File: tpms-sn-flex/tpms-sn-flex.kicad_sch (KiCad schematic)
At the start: 59 parts, among them J1 NRF_CONN, J2 DEBUG_CONN, J3 SMA EDGE CONN, J4 UART_CONN, J5 USER_CAP, J6 PRESSURE_SENSOR_CONN, SW1 SW_Push, U1 STM32U031R8T6

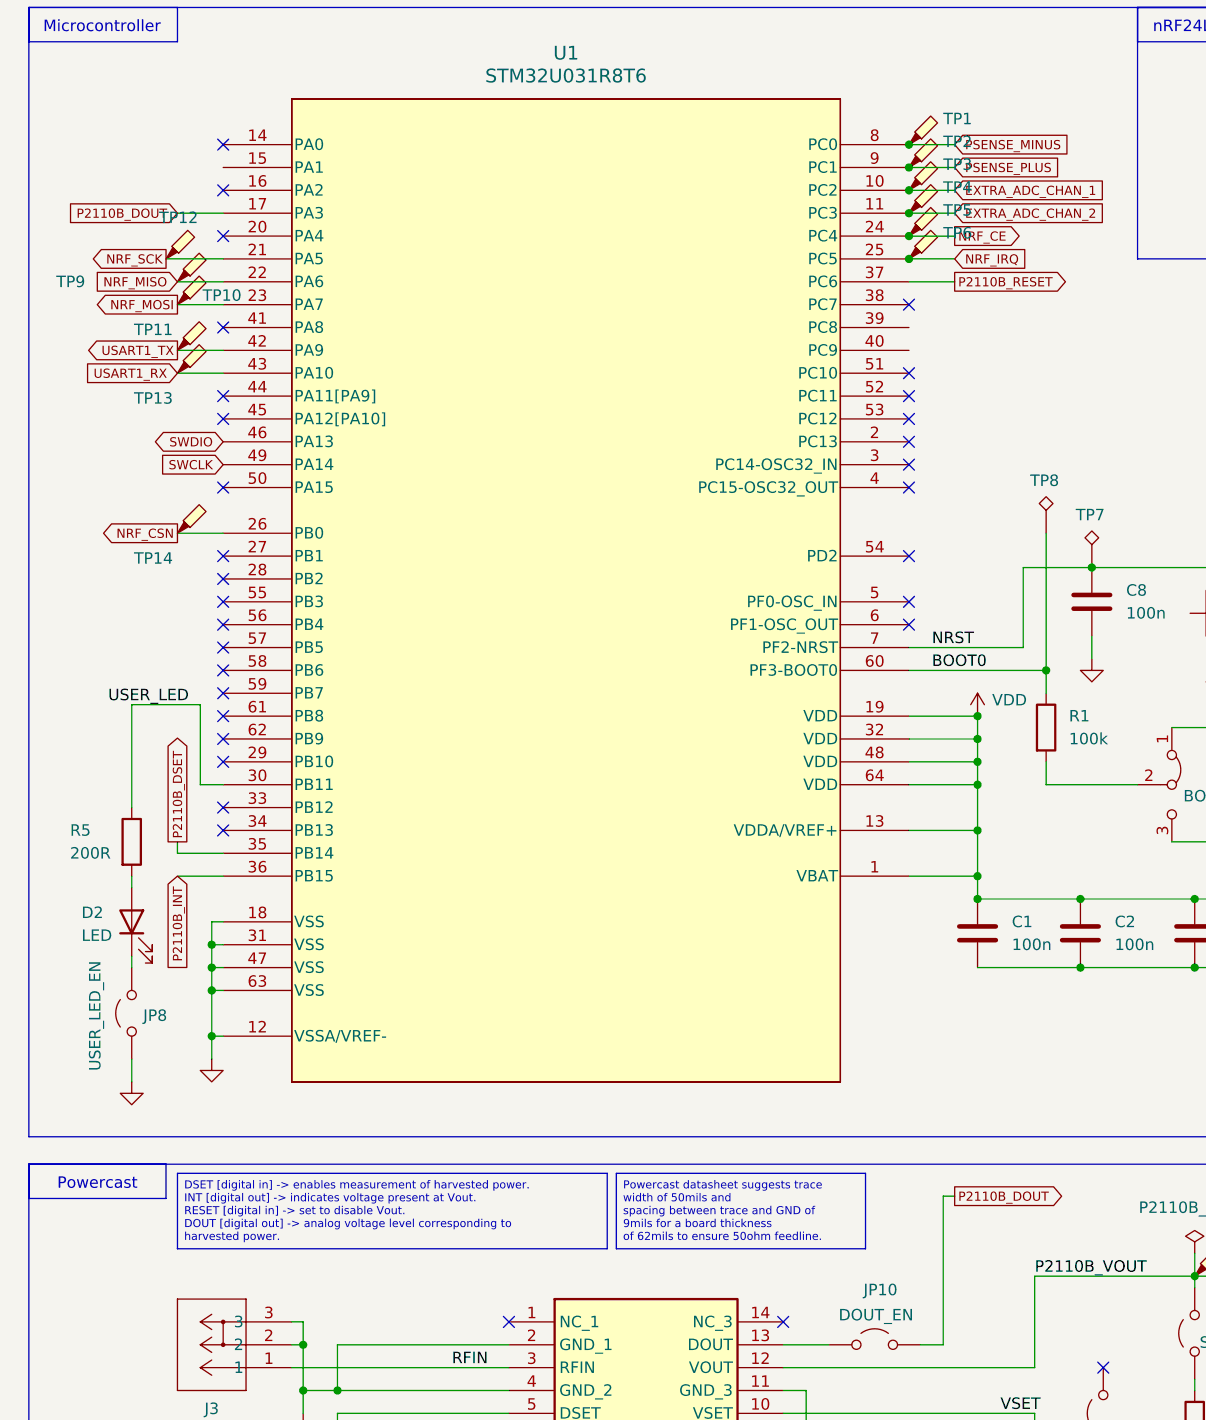
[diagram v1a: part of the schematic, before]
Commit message: Update PCB with silkscreen and fix DRC violations
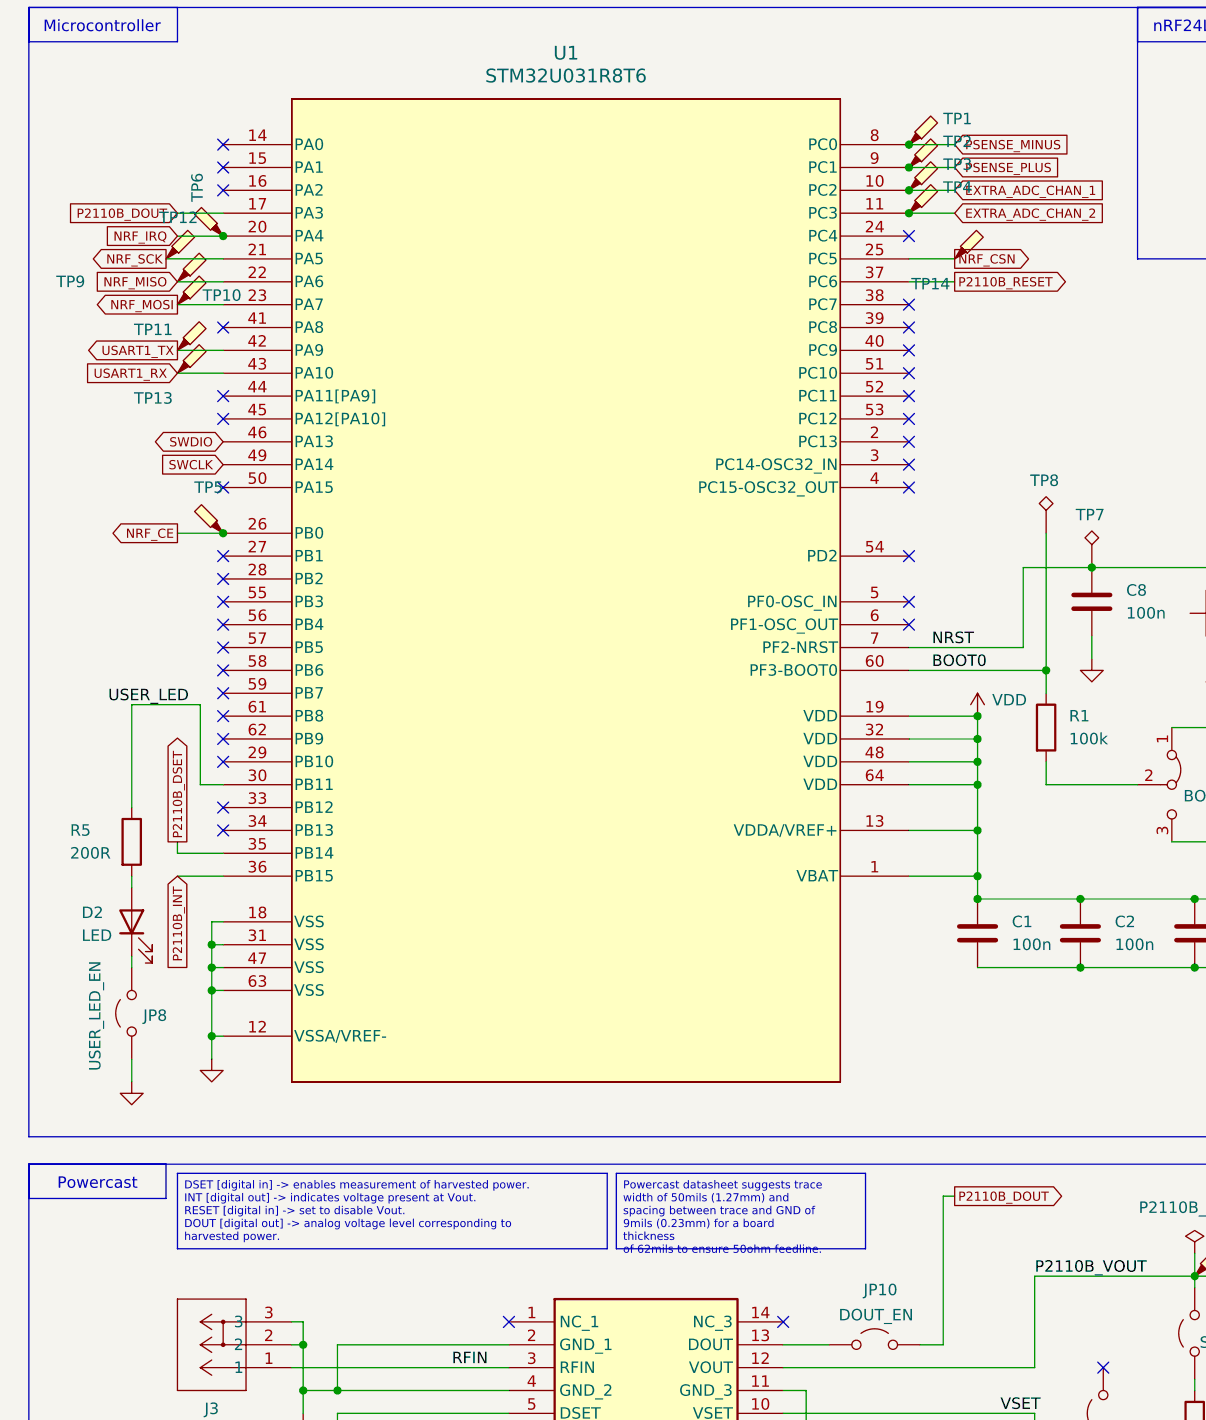
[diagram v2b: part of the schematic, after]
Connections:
- net NRF_CE: now also U1.26 (PB0); no longer U1.24 (PC4)
- net NRF_CSN: now also U1.25 (PC5); no longer U1.26 (PB0)
- net NRF_IRQ: now also U1.20 (PA4); no longer U1.25 (PC5)
- no-connect marks 38 -> 41
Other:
- moved on the sheet: TP14, TP5, TP6
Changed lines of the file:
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@@
 	)
 	(junction
-		(at 111.76 39.37)
-		(diameter 0)
-		(color 0 0 0 0)
-	)
-	(junction
-		(at 111.76 41.91)
-		(diameter 0)
-		(color 0 0 0 0)
-	)
-	(junction
 		(at 119.38 100.33)
 		(diameter 0)
@@
 	)
 	(junction
+		(at 35.56 39.37)
+		(diameter 0)
+		(color 0 0 0 0)
+	)
+	(junction
 		(at 34.29 128.27)
 		(diameter 0)
@@
 	)
 	(junction
+		(at 35.56 72.39)
+		(diameter 0)
+		(color 0 0 0 0)
+	)
+	(junction
 		(at 165.1 113.03)
 		(diameter 0)
@@
 	)
 	(no_connect
+		(at 111.76 49.53)
+	)
+	(no_connect
 		(at 111.76 54.61)
 	)
 	(no_connect
+		(at 111.76 39.37)
+	)
+	(no_connect
 		(at 233.68 34.29)
 	)
@@
 	)
 	(no_connect
-		(at 35.56 39.37)
-	)
-	(no_connect
 		(at 35.56 90.17)
 	)
@@
 	)
 	(no_connect
+		(at 35.56 31.75)
+	)
+	(no_connect
 		(at 208.28 67.31)
 	)
@@
 	)
 	(no_connect
+		(at 111.76 52.07)
+	)
+	(no_connect
 		(at 111.76 82.55)
 	)
@@
 	(wire
 		(pts
-			(xy 111.76 39.37) (xy 116.84 39.37)
+			(xy 35.56 72.39) (xy 30.48 72.39)
 		)
 		(stroke
@@
 	(wire
 		(pts
-			(xy 111.76 41.91) (xy 116.84 41.91)
+			(xy 35.56 39.37) (xy 30.48 39.37)
 		)
 		(stroke
@@
 	(wire
 		(pts
-			(xy 30.48 72.39) (xy 35.56 72.39)
+			(xy 116.84 41.91) (xy 111.76 41.91)
 		)
 		(stroke
@@
 		)
 	)
-	(text_box "Powercast datasheet suggests trace width of 50mils and\nspacing between trace and GND of 9mils for a board thickness\nof 62mils to ensure 50ohm feedline."
+	(text_box "Powercast datasheet suggests trace width of 50mils (1.27mm) and\nspacing between trace and GND of 9mils (0.23mm) for a board thickness\nof 62mils to ensure 50ohm feedline."
 		(exclude_from_sim no)
 		(at 79.248 143.51 0)
@@
 	(global_label "NRF_CE"
 		(shape output)
-		(at 116.84 39.37 0)
+		(at 30.48 72.39 180)
 		(fields_autoplaced yes)
 		(effects
@@
 				(size 1.016 1.016)
 			)
-			(justify left)
+			(justify right)
 		)
 		(property "Intersheetrefs" "${INTERSHEET_REFS}"
-			(at 124.8885 39.37 0)
+			(at 22.4315 72.39 0)
 			(effects
 				(font
 					(size 1.27 1.27)
 				)
-				(justify left)
+				(justify right)
 				(hide yes)
 			)
@@
 	(global_label "NRF_CSN"
 		(shape output)
-		(at 30.48 72.39 180)
+		(at 116.84 41.91 0)
 		(fields_autoplaced yes)
 		(effects
@@
 				(size 1.016 1.016)
 			)
-			(justify right)
+			(justify left)
 		)
 		(property "Intersheetrefs" "${INTERSHEET_REFS}"
-			(at 21.3187 72.39 0)
+			(at 126.0013 41.91 0)
 			(effects
 				(font
 					(size 1.27 1.27)
 				)
-				(justify right)
+				(justify left)
 				(hide yes)
 			)
@@
 	(global_label "NRF_IRQ"
 		(shape input)
-		(at 116.84 41.91 0)
+		(at 30.48 39.37 180)
 		(fields_autoplaced yes)
 		(effects
@@
 				(size 1.016 1.016)
 			)
-			(justify left)
+			(justify right)
 		)
 		(property "Intersheetrefs" "${INTERSHEET_REFS}"
-			(at 125.5175 41.91 0)
+			(at 21.8025 39.37 0)
 			(effects
 				(font
 					(size 1.27 1.27)
 				)
-				(justify left)
+				(justify right)
 				(hide yes)
 			)
@@
 	(symbol
 		(lib_id "Connector:TestPoint_Probe")
-		(at 111.76 39.37 0)
+		(at 35.56 72.39 90)
 		(unit 1)
 		(exclude_from_sim no)
@@
 		(fields_autoplaced yes)
 		(property "Reference" "TP5"
-			(at 115.57 36.5124 0)
+			(at 33.9725 67.31 90)
 			(effects
 				(font
 					(size 1.27 1.27)
 				)
-				(justify left)
 			)
 		)
 		(property "Value" "TestPoint_Probe"
-			(at 115.57 39.0524 0)
+			(at 35.2424 68.58 0)
 			(effects
 				(font
@@
 		)
 		(property "Footprint" "TestPoint:TestPoint_Pad_2.0x2.0mm"
-			(at 116.84 39.37 0)
+			(at 35.56 67.31 0)
 			(effects
 				(font
@@
 		)
 		(property "Datasheet" "~"
-			(at 116.84 39.37 0)
+			(at 35.56 67.31 0)
 			(effects
 				(font
@@
 		)
 		(property "Description" "test point (alternative probe-style design)"
-			(at 111.76 39.37 0)
+			(at 35.56 72.39 0)
 			(effects
 				(font
@@
 	(symbol
 		(lib_id "Connector:TestPoint_Probe")
-		(at 111.76 41.91 0)
+		(at 35.56 39.37 90)
 		(unit 1)
 		(exclude_from_sim no)
@@
 		(on_board yes)
 		(dnp no)
-		(fields_autoplaced yes)
 		(property "Reference" "TP6"
-			(at 115.57 39.0524 0)
+			(at 32.7024 35.56 0)
 			(effects
 				(font
@@
 		)
 		(property "Value" "TestPoint_Probe"
-			(at 115.57 41.5924 0)
+			(at 35.2424 35.56 0)
 			(effects
 				(font
@@
 		)
 		(property "Footprint" "TestPoint:TestPoint_Pad_2.0x2.0mm"
-			(at 116.84 41.91 0)
+			(at 35.56 34.29 0)
 			(effects
 				(font
@@
 		)
 		(property "Datasheet" "~"
-			(at 116.84 41.91 0)
+			(at 35.56 34.29 0)
 			(effects
 				(font
@@
 		)
 		(property "Description" "test point (alternative probe-style design)"
-			(at 111.76 41.91 0)
+			(at 35.56 39.37 0)
 			(effects
 				(font
@@
 	(symbol
 		(lib_id "Connector:TestPoint_Probe")
-		(at 30.48 72.39 0)
+		(at 116.84 41.91 0)
 		(unit 1)
 		(exclude_from_sim no)
@@
 		(dnp no)
 		(property "Reference" "TP14"
-			(at 25.654 75.184 0)
+			(at 112.014 44.704 0)
 			(effects
 				(font
@@
 		)
 		(property "Value" "~"
-			(at 34.29 72.0724 0)
+			(at 120.65 41.5924 0)
 			(effects
 				(font
@@
 		)
 		(property "Footprint" "TestPoint:TestPoint_Pad_2.0x2.0mm"
-			(at 35.56 72.39 0)
+			(at 121.92 41.91 0)
 			(effects
 				(font
@@
 		)
 		(property "Datasheet" "~"
-			(at 35.56 72.39 0)
+			(at 121.92 41.91 0)
 			(effects
 				(font
@@
 		)
 		(property "Description" "test point (alternative probe-style design)"
-			(at 30.48 72.39 0)
+			(at 116.84 41.91 0)
 			(effects
 				(font

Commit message: Fix decoupling caps to be 0603 footprint
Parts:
- C1, C2, C3, C4, C5, C6, C8: footprint Capacitor_SMD:C_01005_0402Metric -> Capacitor_SMD:C_0603_1608Metric
- C7: footprint Capacitor_SMD:C_0201_0603Metric -> Capacitor_SMD:C_0603_1608Metric
- D1, D2: footprint LED_SMD:LED_0402_1005Metric -> LED_SMD:LED_0603_1608Metric
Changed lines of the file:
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@@
 			)
 		)
-		(property "Footprint" "LED_SMD:LED_0402_1005Metric"
+		(property "Footprint" "LED_SMD:LED_0603_1608Metric"
 			(at 25.4 115.57 0)
 			(effects
@@
 			)
 		)
-		(property "Footprint" "Capacitor_SMD:C_0201_0603Metric"
+		(property "Footprint" "Capacitor_SMD:C_0603_1608Metric"
 			(at 187.6552 120.65 0)
 			(effects
@@
 			)
 		)
-		(property "Footprint" "Capacitor_SMD:C_01005_0402Metric"
+		(property "Footprint" "Capacitor_SMD:C_0603_1608Metric"
 			(at 133.0452 83.82 0)
 			(effects
@@
 			)
 		)
-		(property "Footprint" "Capacitor_SMD:C_01005_0402Metric"
+		(property "Footprint" "Capacitor_SMD:C_0603_1608Metric"
 			(at 176.2252 120.65 0)
 			(effects
@@
 			)
 		)
-		(property "Footprint" "Capacitor_SMD:C_01005_0402Metric"
+		(property "Footprint" "Capacitor_SMD:C_0603_1608Metric"
 			(at 131.7752 120.65 0)
 			(effects
@@
 			)
 		)
-		(property "Footprint" "LED_SMD:LED_0402_1005Metric"
+		(property "Footprint" "LED_SMD:LED_0603_1608Metric"
 			(at 247.65 82.55 0)
 			(effects
@@
 			)
 		)
-		(property "Footprint" "Capacitor_SMD:C_01005_0402Metric"
+		(property "Footprint" "Capacitor_SMD:C_0603_1608Metric"
 			(at 155.9052 120.65 0)
 			(effects
@@
 			)
 		)
-		(property "Footprint" "Capacitor_SMD:C_01005_0402Metric"
+		(property "Footprint" "Capacitor_SMD:C_0603_1608Metric"
 			(at 144.4752 120.65 0)
 			(effects
@@
 			)
 		)
-		(property "Footprint" "Capacitor_SMD:C_01005_0402Metric"
+		(property "Footprint" "Capacitor_SMD:C_0603_1608Metric"
 			(at 120.3452 120.65 0)
 			(effects
@@
 			)
 		)
-		(property "Footprint" "Capacitor_SMD:C_01005_0402Metric"
+		(property "Footprint" "Capacitor_SMD:C_0603_1608Metric"
 			(at 166.0652 120.65 0)
 			(effects

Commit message: Add manufacturing files for rev 1
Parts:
- C1, C2, C3, C4, C5, C6, C8: Manufacturer_Part_Number (none) -> KAM15AR71H104KM; Mouser Part Number (none) -> 581-KAM15AR71H104KM
- C7: Manufacturer_Part_Number (none) -> GRM188R60J106KE47J; Mouser Part Number (none) -> 81-GRM188R60J106KE7J
- D1, D2: Manufacturer_Part_Number (none) -> 150060GS55040; Mouser Part Number (none) -> 710-150060GS55040
- H1, H2, H3, H4: footprint MountingHole:MountingHole_2.2mm_M2 -> MountingHole:MountingHole_2.2mm_M2_Pad; symbol Mechanical:MountingHole -> Mechanical:MountingHole_Pad
- J1: Manufacturer_Part_Number (none) -> 90151-2104; Mouser Part Number (none) -> 538-90151-2104
- J3: Manufacturer_Part_Number (none) -> 73251-1150; Mouser Part Number (none) -> 538-73251-1150
- R1: Manufacturer_Part_Number (none) -> ERJ-PA3D1003V; Mouser Part Number (none) -> 667-ERJ-PA3D1003V
- R2: Manufacturer_Part_Number (none) -> CRCW06031M58FKEA; Mouser Part Number (none) -> 71-CRCW06031M58FKEA
- R3: Manufacturer_Part_Number (none) -> ERJ-S03F6043V; Mouser Part Number (none) -> 667-ERJ-S03F6043V
- R4, R5, R6, R7: value 200R -> 220R; Manufacturer_Part_Number (none) -> ERJ-PA3D2200V; Mouser Part Number (none) -> 667-ERJ-PA3D2200V
- SW1: Manufacturer_Part_Number (none) -> B3FS-1002P; Mouser Part Number (none) -> 653-B3FS-1002P
- TP1, TP10, TP11, TP12, TP13, TP14, TP15, TP16, TP2, TP3, TP4, TP5, TP6, TP7, TP8, TP9: Manufacturer_Part_Number (none) -> RCT-0C; Mouser Part Number (none) -> 279-RCT-0C
- U1: Manufacturer_Part_Number (none) -> STM32U031R8T6; Mouser Part Number (none) -> 511-STM32U031R8T6
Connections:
- net GND: now also H1.1, H2.1, H3.1, H4.1
